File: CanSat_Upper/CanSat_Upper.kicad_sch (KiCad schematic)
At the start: 10 parts, among them J1 SERVO1, J2 SERVO1, J3 SERVO1, J4 SERVO1, J5 SERVO1, J6 SERVO1, U1 IST8310, U3 LP5912_500-ma/3.3V

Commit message: Schematic and layout setup finished
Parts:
- removed F10N1: ~, F10_gps:ubx_F10, symbol GPS:_1
- removed U3: LP5912_500-ma/3.3V, CanSat:LP5912-LDO, symbol LDO:LP5912_LDO
- added C1, C2, C3, C4: 10u, Capacitor_SMD:C_0603_1608Metric, symbol Device:C
- added C10, C5, C6, C8, C9: 100n, Capacitor_SMD:C_0603_1608Metric, symbol Device:C
- added C7: 4.7u, Capacitor_SMD:C_0603_1608Metric, symbol Device:C
- added H1, H2, H3, H4: MountingHole, MountingHole:MountingHole_2mm, symbol Mechanical:MountingHole
- added J10: Power GND, Connector_Wire:SolderWirePad_1x01_SMD_4x8mm, symbol Connector:Conn_01x01_Socket
- added J7: Power 5V, Connector_Wire:SolderWirePad_1x01_SMD_4x8mm, symbol Connector:Conn_01x01_Socket
- added J8: JST_SH_10pin, Connector_JST:JST_SH_SM10B-SRSS-TB_1x10-1MP_P1.00mm_Horizontal, symbol Connector:Conn_01x10_Socket
- added J9: JST_SH_8pin, Connector_JST:JST_SH_SM08B-SRSS-TB_1x08-1MP_P1.00mm_Horizontal, symbol Connector:Conn_01x08_Socket
- added R1, R2: 10k, Resistor_SMD:R_0603_1608Metric, symbol Device:R
- added R3, R4: 4.7k, Resistor_SMD:R_0603_1608Metric, symbol Device:R
- added U3: F10N1, GPS:ubx_F10, symbol GPS:_1
- added U4, U5: LP5912_500-ma/3.3V, LDO:LP5912-LDO, symbol LDO:LP5912_LDO
- U1: footprint CanSat:IST8310 LGA -> Magnetometer:IST8310 LGA
- U2: value ~ -> XBee3; footprint (none) -> XBee:XBee3
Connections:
- net +5V: now also C1.1, C3.1, J7.1 (Pin_1), U4.4 (EN), U4.6 (IN), U5.4 (EN), U5.6 (IN)
- net GND: now also U1.11 (GND), U1.5 (CAD0), U1.6 (CAD1), U1.9 (GND), U2.10 (GND), C1.2, C10.2, C2.2, C3.2, C4.2, C5.2, C6.2, C7.2, C8.2, C9.2, J10.1 (Pin_1), J8.10 (Pin_10), J8.2 (Pin_2), J8.4 (Pin_4), J8.7 (Pin_7), J9.3 (Pin_3), J9.6 (Pin_6), U3.1 (GND), U3.13 (GND), U3.14 (GND), U3.15 (GND), U3.19 (GND), U3.2 (GND), U3.21 (GND), U3.22 (GND), U3.23 (GND), U3.26 (GND), U3.27 (GND), U3.28 (GND), U3.29 (GND), U3.3 (GND), U3.30 (GND), U3.33 (GND), U3.35 (GND), U3.37 (GND), U3.38 (GND), U3.4 (GND), U3.40 (GND), U3.41 (GND), U3.42 (GND), U3.43 (GND), U3.44 (GND), U3.47 (GND), U3.48 (GND), U3.49 (GND), U3.5 (GND), U3.50 (GND), U3.51 (GND), U3.54 (GND), U3.56 (GND), U3.57 (GNDM), U3.6 (GND), U3.7 (GND), U3.8 (GND), U4.5 (GND), U5.5 (GND)
- net S1: now also J9.1 (Pin_1)
- net S2: now also J9.2 (Pin_2)
- net S3: now also J3.1 (Pin_1), J9.4 (Pin_4); no longer J5.1 (Pin_1)
- net S4: now also J9.5 (Pin_5)
- net S5: now also J5.1 (Pin_1), J9.7 (Pin_7); no longer J3.1 (Pin_1)
- net S6: now also J9.8 (Pin_8)
- net SCL: now reaches U1.1 (SCL)
- net SCL: now also J8.3 (Pin_3), R3.2
- net at U1.10 (C1): now also C7.1
- net +3.3V2: now reaches U1.13 (DVDD)
- net +3.3V2: now also U1.2 (AVDD), U2.1 (VCC), C10.1, C4.1, C8.1, C9.1, R2.2, R3.1, R4.1, U5.1 (OUT)
- net SDA: now reaches U1.16 (SDA)
- net SDA: now also J8.1 (Pin_1), R4.2
- net XBEE_TX: now reaches U2.2 (DOUT/DIO13)
- net XBEE_TX: now also J8.5 (Pin_5)
- net XBEE_RX: now reaches U2.3 (DIN/~{CONFIG}/DIO14)
- net XBEE_RX: now also J8.6 (Pin_6)
- new net: R2.1, U5.3 (PG)
- new net: R1.1, U4.3 (PG)
- new net +3.3V1: C2.1, C5.1, C6.1, R1.2, U3.52 (VCC), U3.53 (VCC), U4.1 (OUT)
- new net GPS_RX: J8.9 (Pin_9), U3.9 (RX)
- new net GPS_TX: J8.8 (Pin_8), U3.10 (TX)
- no-connect marks 0 -> 31
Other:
- note added: "Connectors"
- note added: "GPS"
- note added: "KiCad Stuff"
- note added: "Magnetometer"
- note added: "Power"
- moved on the sheet: J1, J2, J3, J4, J5, J6

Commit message: general PBC layout done
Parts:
- removed C10: 100n, Capacitor_SMD:C_0603_1608Metric, symbol Device:C
- removed R2: 10k, Resistor_SMD:R_0603_1608Metric, symbol Device:R
- removed U5: LP5912_500-ma/3.3V, LDO:LP5912-LDO, symbol LDO:LP5912_LDO
- added D1, D2, D3, D4: TVS, Diode_SMD:D_0402_1005Metric, symbol Diode:ESD5Zxx
- C3: value 10u -> 1u
- C4: value 10u -> 8.2p
- J10, J7: footprint Connector_Wire:SolderWirePad_1x01_SMD_4x8mm -> Connector_Wire:SolderWirePad_1x01_SMD_3x6mm
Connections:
- net +3.3V2 is gone; now on net +3.3V: C4.1, C8.1, C9.1, R3.1, R4.1, U1.13 (DVDD), U1.2 (AVDD), U2.1 (VCC)
- net +5V: no longer C3.1
- net GND: now also D1.2 (A), D2.2 (A), D3.2 (A), D4.2 (A)
- net GPS_RX: now also J8.8 (Pin_8), D3.1 (K); no longer J8.9 (Pin_9)
- net GPS_TX: now also J8.9 (Pin_9), D4.1 (K); no longer J8.8 (Pin_8)
- net SCL: now also D1.1 (K)
- net SDA: now also D2.1 (K)
- net +3.3V1 renamed +3.3V
- net +3.3V: now also C3.1
- no-connect marks 31 -> 30
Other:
- note added: "XBee 3 Radio 2.4GHz"

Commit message: v0.1 finished
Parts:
- R3, R4: value 4.7k -> 10k
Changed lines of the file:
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@@
 			)
 		)
-		(property "Value" "4.7k"
+		(property "Value" "10k"
 			(at 287.02 259.0799 0)
 			(effects
@@
 			)
 		)
-		(property "Value" "4.7k"
+		(property "Value" "10k"
 			(at 278.13 259.0799 0)
 			(effects

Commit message: Added variations of the magnetometers power supply
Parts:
- removed D3, D4: TVS, Diode_SMD:D_0402_1005Metric, symbol Diode:ESD5Zxx
- removed R4: 10k, Resistor_SMD:R_0603_1608Metric, symbol Device:R
- added C10, C11, C12, C13: 1u, Capacitor_SMD:C_0603_1608Metric, symbol Device:C
- added R2, R5, R6: 0, Resistor_SMD:R_0603_1608Metric, symbol Device:R
- added U5, U6: TPS77033PDBV, Package_TO_SOT_SMD:SOT-23-5, symbol Regulator_Linear:TPS77033PDBV
- R3: value 10k -> 0
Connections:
- net +3.3V: now also R2.1; no longer C8.1, C9.1, R3.1, U1.13 (DVDD), U1.2 (AVDD)
- net +5V: now also C10.1, C12.1, U5.1 (IN), U5.3 (EN), U6.1 (IN), U6.3 (EN)
- net GND: now also C10.2, C11.2, C12.2, C13.2, U5.2 (GND), U5.4 (GND), U6.2 (GND), U6.4 (GND)
- net SCL: no longer R3.2
- new net: C9.1, R3.2, R6.2, U1.2 (AVDD)
- new net: C8.1, R2.2, R3.1, R5.2, U1.13 (DVDD)
- new net +3.3V2: C11.1, R5.1, U5.5 (OUT)
- new net +3.3V3: C13.1, R6.1, U6.5 (OUT)
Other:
- moved on the sheet: C9

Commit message: v0.2 done
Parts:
- added C14, C15, C16: ?, Capacitor_SMD:C_0603_1608Metric, symbol Device:C
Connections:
- net +5V: now also C14.1, C15.1, C16.1
- net GND: now also C14.2, C15.2, C16.2

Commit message: quick fixes to v0.2
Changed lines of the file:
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@@
 	)
 	(junction
+		(at 292.1 299.72)
+		(diameter 0)
+		(color 0 0 0 0)
+	)
+	(junction
 		(at 119.38 262.89)
 		(diameter 0)
@@
 	)
 	(junction
+		(at 303.53 262.89)
+		(diameter 0)
+		(color 0 0 0 0)
+	)
+	(junction
 		(at 303.53 247.65)
 		(diameter 0)
@@
 	(wire
 		(pts
-			(xy 292.1 299.72) (xy 284.48 299.72)
-		)
-		(stroke
-			(width 0)
-			(type default)
-		)
-	)
-	(wire
-		(pts
 			(xy 133.35 316.23) (xy 137.16 316.23)
 		)
@@
 	(wire
 		(pts
+			(xy 303.53 262.89) (xy 303.53 266.7)
+		)
+		(stroke
+			(width 0)
+			(type default)
+		)
+	)
+	(wire
+		(pts
 			(xy 152.4 316.23) (xy 161.29 316.23)
 		)
@@
 	(wire
 		(pts
+			(xy 284.48 299.72) (xy 292.1 299.72)
+		)
+		(stroke
+			(width 0)
+			(type default)
+		)
+	)
+	(wire
+		(pts
 			(xy 116.84 143.51) (xy 121.92 143.51)
 		)
@@
 	(wire
 		(pts
-			(xy 303.53 247.65) (xy 303.53 266.7)
+			(xy 303.53 247.65) (xy 303.53 262.89)
 		)
 		(stroke
@@
 	)
 	(symbol
+		(lib_id "power:PWR_FLAG")
+		(at 303.53 262.89 270)
+		(unit 1)
+		(exclude_from_sim no)
+		(in_bom yes)
+		(on_board yes)
+		(dnp no)
+		(fields_autoplaced yes)
+		(property "Reference" "#FLG03"
+			(at 305.435 262.89 0)
+			(effects
+				(font
+					(size 1.27 1.27)
+				)
+				(hide yes)
+			)
+		)
+		(property "Value" "PWR_FLAG"
+			(at 307.34 262.8899 90)
+			(effects
+				(font
+					(size 1.27 1.27)
+				)
+				(justify left)
+			)
+		)
+		(property "Footprint" ""
+			(at 303.53 262.89 0)
+			(effects
+				(font
+					(size 1.27 1.27)
+				)
+				(hide yes)
+			)
+		)
+		(property "Datasheet" "~"
+			(at 303.53 262.89 0)
+			(effects
+				(font
+					(size 1.27 1.27)
+				)
+				(hide yes)
+			)
+		)
+		(property "Description" "Special symbol for telling ERC where power comes from"
+			(at 303.53 262.89 0)
+			(effects
+				(font
+					(size 1.27 1.27)
+				)
+				(hide yes)
+			)
+		)
+		(pin "1"
+		)
+		(instances
+			(project ""
+				(path "/e536c02a-70cd-4fec-a52a-e0d1e5651a32"
+					(reference "#FLG03")
+					(unit 1)
+				)
+			)
+		)
+	)
+	(symbol
 		(lib_id "power:GND")
 		(at 309.88 257.81 0)
@@
 	)
 	(symbol
+		(lib_id "power:PWR_FLAG")
+		(at 292.1 299.72 180)
+		(unit 1)
+		(exclude_from_sim no)
+		(in_bom yes)
+		(on_board yes)
+		(dnp no)
+		(fields_autoplaced yes)
+		(property "Reference" "#FLG04"
+			(at 292.1 301.625 0)
+			(effects
+				(font
+					(size 1.27 1.27)
+				)
+				(hide yes)
+			)
+		)
+		(property "Value" "PWR_FLAG"
+			(at 292.1 304.8 0)
+			(effects
+				(font
+					(size 1.27 1.27)
+				)
+			)
+		)
+		(property "Footprint" ""
+			(at 292.1 299.72 0)
+			(effects
+				(font
+					(size 1.27 1.27)
+				)
+				(hide yes)
+			)
+		)
+		(property "Datasheet" "~"
+			(at 292.1 299.72 0)
+			(effects
+				(font
+					(size 1.27 1.27)
+				)
+				(hide yes)
+			)
+		)
+		(property "Description" "Special symbol for telling ERC where power comes from"
+			(at 292.1 299.72 0)
+			(effects
+				(font
+					(size 1.27 1.27)
+				)
+				(hide yes)
+			)
+		)
+		(pin "1"
+		)
+		(instances
+			(project "CanSat_Upper"
+				(path "/e536c02a-70cd-4fec-a52a-e0d1e5651a32"
+					(reference "#FLG04")
+					(unit 1)
+				)
+			)
+		)
+	)
+	(symbol
 		(lib_id "power:GND")
 		(at 499.11 245.11 0)
@@
 		(on_board yes)
 		(dnp no)
-		(fields_autoplaced yes)
 		(property "Reference" "#PWR038"
 			(at 276.86 290.83 0)
@@
 		)
 		(property "Value" "+3.3V3"
-			(at 276.86 281.94 0)
+			(at 276.86 282.956 0)
 			(effects
 				(font

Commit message: production files done
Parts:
- C1, C2: LCSC (none) -> C596327
- C10, C11, C12, C13, C3: LCSC (none) -> C77046
- C14, C15, C16: value ? -> 1u; LCSC (none) -> C77046
- C4: LCSC (none) -> C962145
- C5, C6, C8, C9: LCSC (none) -> C77055
- C7: LCSC (none) -> C327022
- D1, D2: LCSC (none) -> C1869319
- J1, J2, J3, J4, J5, J6: LCSC (none) -> C265013
- J8: LCSC (none) -> C160409
- J9: LCSC (none) -> C160407
- R1: LCSC (none) -> C844918
- R2, R3, R5, R6: LCSC (none) -> C95177
- U5, U6: LCSC (none) -> C36996065

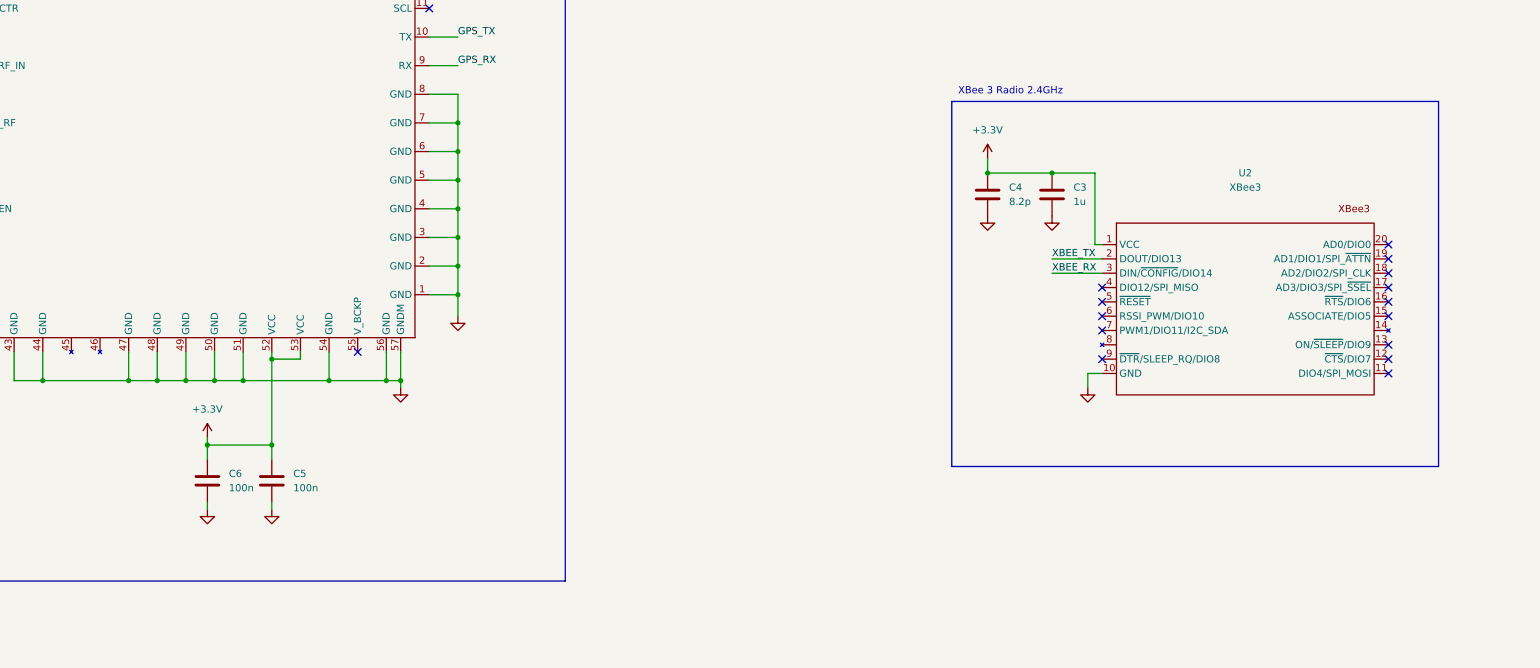
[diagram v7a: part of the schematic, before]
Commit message: small fixes, added 0resistors to turn on/off radio modeules power
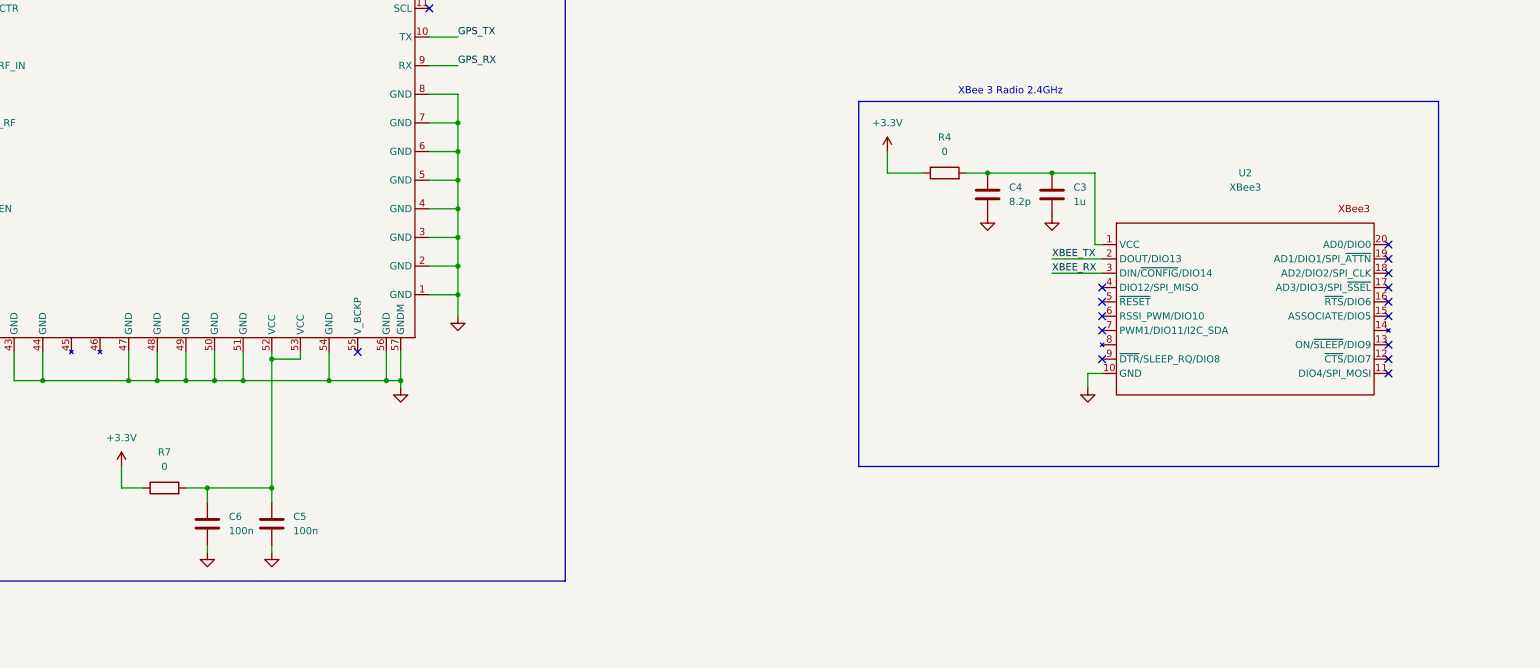
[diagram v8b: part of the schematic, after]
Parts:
- added R4, R7: 0, Resistor_SMD:R_0603_1608Metric, symbol Device:R
- U1: LCSC number C2683055 -> C2683055
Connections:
- net +3.3V: now also R4.1, R7.1; no longer C3.1, C4.1, C5.1, C6.1, U2.1 (VCC), U3.52 (VCC), U3.53 (VCC)
- new net: C5.1, C6.1, R7.2, U3.52 (VCC), U3.53 (VCC)
- new net: C3.1, C4.1, R4.2, U2.1 (VCC)
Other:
- moved on the sheet: C5, C6
